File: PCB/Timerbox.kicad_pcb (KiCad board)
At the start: 2 copper layers, 97 x 49 mm, 29 parts, among them CON1 AVR-ISP-6, IC1 ATTINY4313-P, K1 ROT, P1 CON, P2 BTN1, P4 RST, P5 BTN0, Q1 2N3904, U1 78L05, U2 LM7812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

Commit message: New PCB
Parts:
- removed D2: LED, LED-5MM
- removed the HOLE at (169.5, 97.5)
- removed the HOLE at (169.5, 136.5)
- removed the HOLE at (257.5, 136.5)
- removed K1: ROT, PIN_ARRAY_3X1
- removed R6: 510, R3
- removed R7: 1k, R3
- added HOLE: Val**, HOLE_28, F.Cu at (169.0, 138.0)
- added HOLE: Val**, HOLE_28, F.Cu at (169.0, 97.0)
- added HOLE: Val**, HOLE_28, F.Cu at (258.0, 138.0)
- added P3: BTN2, PIN_ARRAY_2X1, F.Cu at (259.0, 131.8)
- added P6: BTN3, PIN_ARRAY_2X1, F.Cu at (259.0, 126.0)
- added P7: BTN3, PIN_ARRAY_2X1, F.Cu at (199.0, 116.5)
- added P8: BTN4, PIN_ARRAY_2X1, F.Cu at (221.0, 104.0)
- added RV1: 10k, R_TRIM_3362P, F.Cu at (229.0, 131.0)
- moved P2 1.00 mm to (259.0, 120.0)
- moved P5 0.50 mm to (259.0, 114.0)
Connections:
- net /SCK renamed /BTN4
- net N-000002 renamed /BTN0
- IC1 pad 13: N-000003 (its old number) -> /BTN1
- IC1 pad 6: /ROT0 -> /BTN2
- IC1 pad 7: /ROT1 -> /BTN3
- IC1 pad 9: N-0000022 -> /BTN5
- P5 pad 1: N-000003 (its old number) -> /BTN1
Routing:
- net /BTN1: track 0.00 -> 94.2 mm
- net N-000003 (its old number): track 89.6 -> 0.00 mm
- net /BTN3: track 0.00 -> 71.9 mm
- net /BTN2: track 0.00 -> 71.0 mm
- net /ROT1: track 65.6 -> 0.00 mm
- net /ROT0: track 57.7 -> 0.00 mm, vias 1 -> 0
- net /BTN5: track 0.00 -> 8.08 mm
- net /BTN4: track 23.2 -> 30.7 mm
- net N-0000022: track 5.94 -> 0.00 mm
- net N-0000021: track 3.94 -> 0.00 mm
- net N-000003: track 10.3 -> 12.6 mm
- net /BTN0: track 86.6 -> 88.2 mm
- net /DB7: track 54.7 -> 55.8 mm, vias 1 -> 0
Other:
- board text added: "Gabriel Fornaeus © Timerbox 0.2 2014"
- board text removed: "Gabriel Fornaeus © Timerbox 0.1 2014"

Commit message: Redid the pcb
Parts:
- added HOLE: Val**, HOLE_30, F.Cu at (258.0, 97.0)
- moved P8 38.3 mm to (259.1, 108.0), turned to 90 degrees
- moved REL1 4.76 mm to (243.2, 103.2)
- moved D1 3.29 mm to (232.8, 104.5)
- moved Q1 3.26 mm to (228.8, 100.2)
- moved R4 2.05 mm to (221.0, 100.3)
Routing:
- net /BTN5: track 8.08 -> 49.6 mm
- net /DB7: track 55.8 -> 76.4 mm
- net /BTN2: track 71.0 -> 56.8 mm
- net +12V: track 122.7 -> 109.7 mm
- net /BTN3: track 71.9 -> 61.5 mm
- net /BTN0: track 88.2 -> 94.0 mm
- net /RL1: track 88.5 -> 83.2 mm
- net +5V: track 155.3 -> 151.1 mm
- net N-0000025: track 13.8 -> 11.0 mm
- net /BTN1: track 94.2 -> 96.5 mm
- net N-000004: track 18.2 -> 16.4 mm
- net N-0000020: track 5.19 -> 3.99 mm
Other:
- board text added: "Gabriel Fornaeus © Timerbox 0.2 2015"
- board text removed: "Gabriel Fornaeus © Timerbox 0.2 2014"

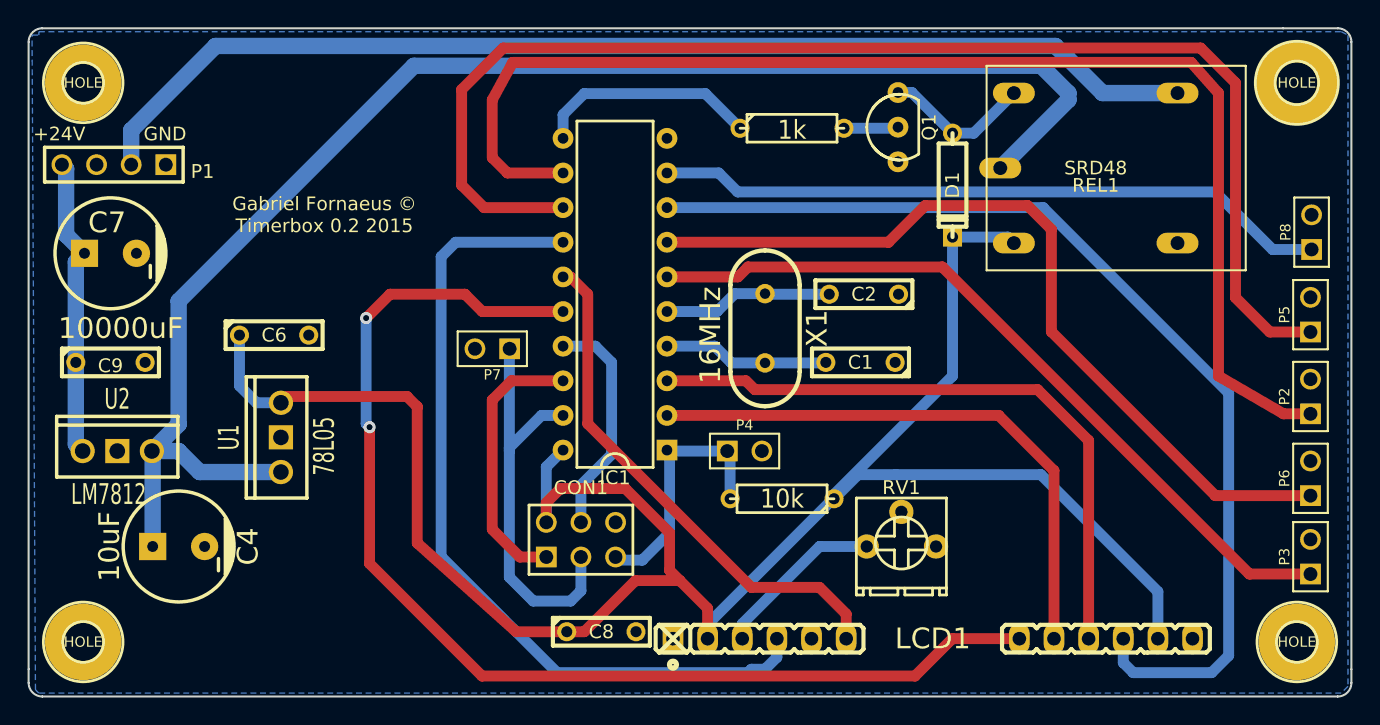
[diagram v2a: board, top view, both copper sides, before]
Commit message: Changed contrast pot
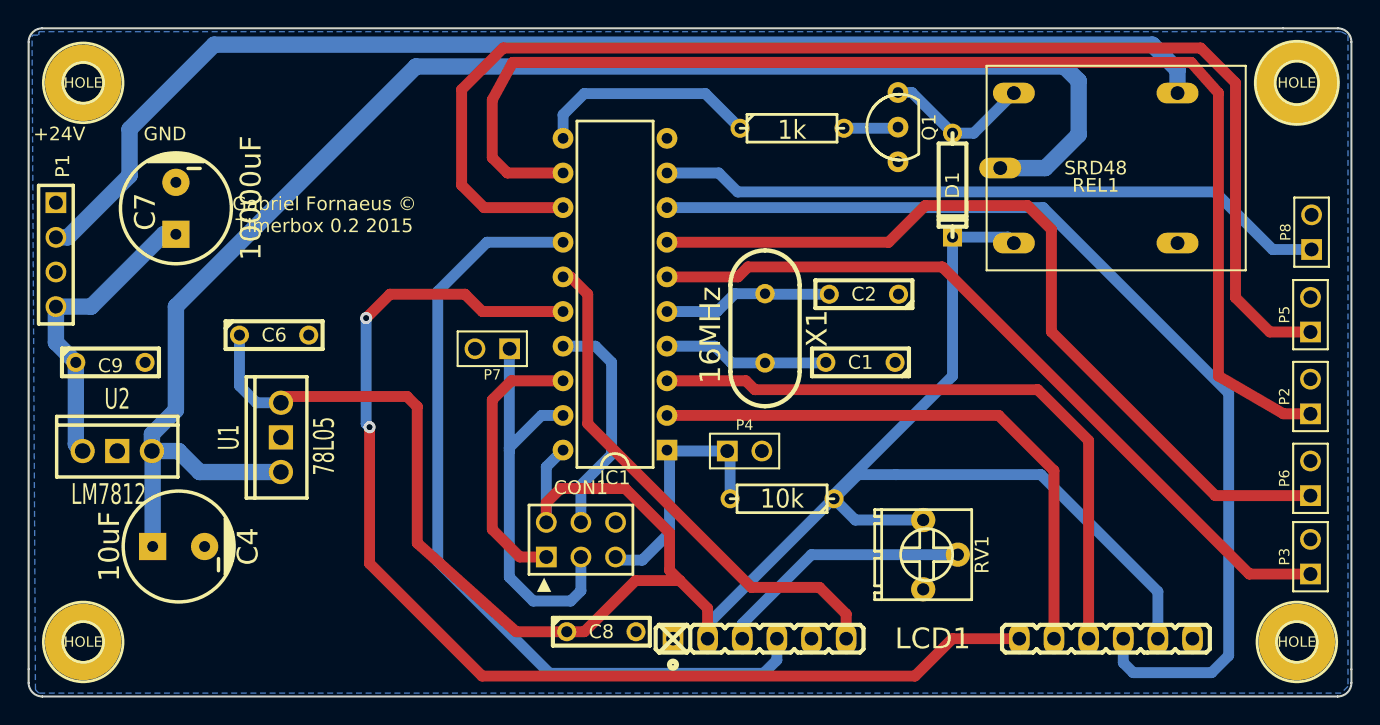
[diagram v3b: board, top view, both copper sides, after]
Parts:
- moved P1 7.85 mm to (167.0, 109.6), turned to 270 degrees
- moved C7 5.82 mm to (175.8, 106.2), turned to 0 degrees
- moved RV1 1.71 mm to (230.6, 131.6), turned to 270 degrees
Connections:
- LCD1 pad 3: N-000003 -> N-0000017
- RV1 pad 1: N-000003 -> +5V
- RV1 pad 2: GND -> N-0000017
- RV1 pad 3: (no net) -> GND
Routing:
- net N-0000017: track 0.00 -> 19.0 mm
- net N-000003: track 12.6 -> 0.00 mm
- net /RL1: track 83.2 -> 92.6 mm
- net +5V: track 151.1 -> 158.3 mm
- net +12V: track 109.7 -> 113.1 mm
- net /RS: track 61.4 -> 60.7 mm
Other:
- board text added: "▲"
